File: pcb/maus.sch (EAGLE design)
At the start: 88 parts, among them Q1 BSS123, Q2 BSS123, Q3 BSS123, Q4 BSS123, Q5 BSS123, Q6 SI3499DV-T1-BE3, Q7 SI3499DV-T1-BE3, U1 ESP32-S2-WROOM, U2 CH340C, U3 CP2102, U4 LP3965EMP-3.3, U5 LSM9DS1TR, U6 LM358DR

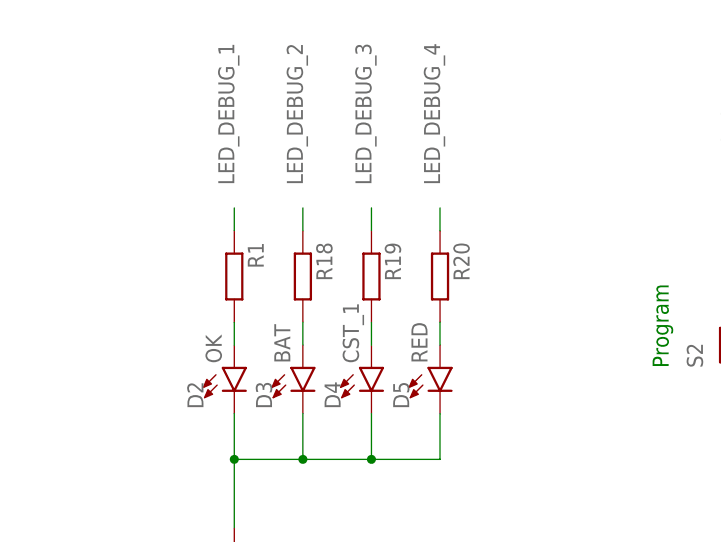
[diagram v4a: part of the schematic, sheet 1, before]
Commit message: set led resistors to 1k, fixes #10
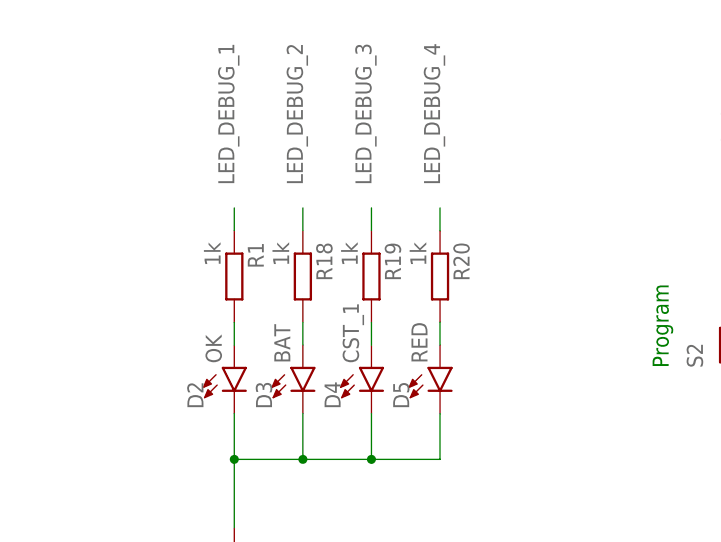
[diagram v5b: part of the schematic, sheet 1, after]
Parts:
- R1, R18, R19, R20: value (none) -> 1k
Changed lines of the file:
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@@
 <drawing>
 <settings>
-<setting alwaysvectorfont="yes"/>
+<setting alwaysvectorfont="no"/>
 <setting verticaltext="up"/>
 </settings>
@@
 <part name="D2" library="SparkFun-LED" library_urn="urn:adsk.eagle:library:529" deviceset="LED-RED" device="0603" package3d_urn="urn:adsk.eagle:package:39354/1" value="OK"/>
 <part name="GND26" library="supply1" library_urn="urn:adsk.eagle:library:371" deviceset="GND" device=""/>
-<part name="R1" library="rcl" library_urn="urn:adsk.eagle:library:334" deviceset="R-EU_" device="R0805" package3d_urn="urn:adsk.eagle:package:23553/2"/>
-<part name="R18" library="rcl" library_urn="urn:adsk.eagle:library:334" deviceset="R-EU_" device="R0805" package3d_urn="urn:adsk.eagle:package:23553/2"/>
+<part name="R1" library="rcl" library_urn="urn:adsk.eagle:library:334" deviceset="R-EU_" device="R0805" package3d_urn="urn:adsk.eagle:package:23553/2" value="1k"/>
+<part name="R18" library="rcl" library_urn="urn:adsk.eagle:library:334" deviceset="R-EU_" device="R0805" package3d_urn="urn:adsk.eagle:package:23553/2" value="1k"/>
 <part name="D3" library="SparkFun-LED" library_urn="urn:adsk.eagle:library:529" deviceset="LED-RED" device="0603" package3d_urn="urn:adsk.eagle:package:39354/1" value="BAT"/>
-<part name="R19" library="rcl" library_urn="urn:adsk.eagle:library:334" deviceset="R-EU_" device="R0805" package3d_urn="urn:adsk.eagle:package:23553/2"/>
+<part name="R19" library="rcl" library_urn="urn:adsk.eagle:library:334" deviceset="R-EU_" device="R0805" package3d_urn="urn:adsk.eagle:package:23553/2" value="1k"/>
 <part name="D4" library="SparkFun-LED" library_urn="urn:adsk.eagle:library:529" deviceset="LED-RED" device="0603" package3d_urn="urn:adsk.eagle:package:39354/1" value="CST_1"/>
-<part name="R20" library="rcl" library_urn="urn:adsk.eagle:library:334" deviceset="R-EU_" device="R0805" package3d_urn="urn:adsk.eagle:package:23553/2"/>
+<part name="R20" library="rcl" library_urn="urn:adsk.eagle:library:334" deviceset="R-EU_" device="R0805" package3d_urn="urn:adsk.eagle:package:23553/2" value="1k"/>
 <part name="D5" library="SparkFun-LED" library_urn="urn:adsk.eagle:library:529" deviceset="LED-RED" device="0603" package3d_urn="urn:adsk.eagle:package:39354/1" value="RED"/>
 <part name="C27" library="rcl" library_urn="urn:adsk.eagle:library:334" deviceset="C-EU" device="C0805" package3d_urn="urn:adsk.eagle:package:23617/2" value="0.1uF/16V"/>

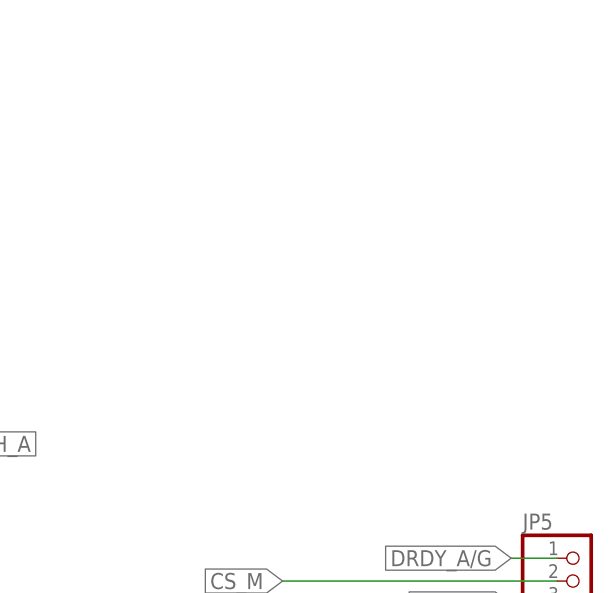
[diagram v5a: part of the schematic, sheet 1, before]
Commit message: added a SPI breakout
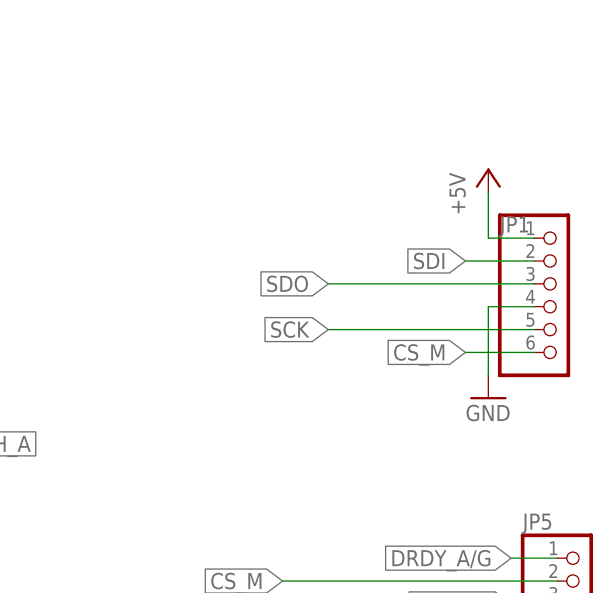
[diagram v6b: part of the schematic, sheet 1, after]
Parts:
- added JP1: (no value), pinhead:PINHD-1X6
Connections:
- net +5V: now also JP1.1
- net CS_M: now also JP1.6
- net GND: now also JP1.4
- net SCK: now also JP1.5
- net SDI: now also JP1.2
- net SDO: now also JP1.3
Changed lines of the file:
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@@
 <part name="C2" library="rcl" library_urn="urn:adsk.eagle:library:334" deviceset="C-EU" device="C0805" package3d_urn="urn:adsk.eagle:package:23617/2" value="100nF"/>
 <part name="GND40" library="supply1" library_urn="urn:adsk.eagle:library:371" deviceset="GND" device=""/>
+<part name="JP1" library="pinhead" library_urn="urn:adsk.eagle:library:325" deviceset="PINHD-1X6" device="" package3d_urn="urn:adsk.eagle:package:22472/2"/>
+<part name="P+8" library="supply1" library_urn="urn:adsk.eagle:library:371" deviceset="+5V" device=""/>
+<part name="GND43" library="supply1" library_urn="urn:adsk.eagle:library:371" deviceset="GND" device=""/>
 </parts>
 <sheets>
@@
 <instance part="+3V12" gate="G$1" x="139.7" y="200.66" smashed="yes">
 <attribute name="VALUE" x="137.16" y="195.58" size="1.778" layer="96" rot="R90"/>
+</instance>
+<instance part="JP1" gate="A" x="233.68" y="88.9" smashed="yes">
+<attribute name="NAME" x="227.33" y="97.155" size="1.778" layer="95"/>
+<attribute name="VALUE" x="227.33" y="78.74" size="1.778" layer="96"/>
+</instance>
+<instance part="P+8" gate="1" x="226.06" y="104.14" smashed="yes">
+<attribute name="VALUE" x="223.52" y="99.06" size="1.778" layer="96" rot="R90"/>
+</instance>
+<instance part="GND43" gate="1" x="226.06" y="78.74" smashed="yes">
+<attribute name="VALUE" x="223.52" y="76.2" size="1.778" layer="96"/>
 </instance>
 </instances>
@@
 <junction x="139.7" y="167.64"/>
 </segment>
+<segment>
+<pinref part="GND43" gate="1" pin="GND"/>
+<wire x1="226.06" y1="88.9" x2="226.06" y2="81.28" width="0.1524" layer="91"/>
+<pinref part="JP1" gate="A" pin="4"/>
+<wire x1="226.06" y1="88.9" x2="231.14" y2="88.9" width="0.1524" layer="91"/>
+</segment>
 </net>
 <net name="ESP32_EN" class="0">
@@
 <label x="119.38" y="58.42" size="1.778" layer="95" xref="yes"/>
 </segment>
+<segment>
+<pinref part="JP1" gate="A" pin="5"/>
+<wire x1="231.14" y1="86.36" x2="208.28" y2="86.36" width="0.1524" layer="91"/>
+<label x="208.28" y="86.36" size="1.778" layer="95" rot="R180" xref="yes"/>
+</segment>
 </net>
 <net name="SDO" class="0">
@@
 <label x="137.16" y="55.88" size="1.778" layer="95" xref="yes"/>
 </segment>
+<segment>
+<pinref part="JP1" gate="A" pin="3"/>
+<wire x1="231.14" y1="91.44" x2="208.28" y2="91.44" width="0.1524" layer="91"/>
+<label x="208.28" y="91.44" size="1.778" layer="95" rot="R180" xref="yes"/>
+</segment>
 </net>
 <net name="SDI" class="0">
@@
 <label x="137.16" y="60.96" size="1.778" layer="95" xref="yes"/>
 </segment>
+<segment>
+<pinref part="JP1" gate="A" pin="2"/>
+<wire x1="231.14" y1="93.98" x2="223.52" y2="93.98" width="0.1524" layer="91"/>
+<label x="223.52" y="93.98" size="1.778" layer="95" rot="R180" xref="yes"/>
+</segment>
 </net>
 <net name="INT" class="0">
@@
 <label x="203.2" y="58.42" size="1.778" layer="95" rot="R180" xref="yes"/>
 <wire x1="233.68" y1="58.42" x2="203.2" y2="58.42" width="0.1524" layer="91"/>
+</segment>
+<segment>
+<pinref part="JP1" gate="A" pin="6"/>
+<wire x1="231.14" y1="83.82" x2="223.52" y2="83.82" width="0.1524" layer="91"/>
+<label x="223.52" y="83.82" size="1.778" layer="95" rot="R180" xref="yes"/>
 </segment>
 </net>
@@
 </segment>
 </net>
+<net name="+5V" class="0">
+<segment>
+<pinref part="JP1" gate="A" pin="1"/>
+<pinref part="P+8" gate="1" pin="+5V"/>
+<wire x1="231.14" y1="96.52" x2="226.06" y2="96.52" width="0.1524" layer="91"/>
+<wire x1="226.06" y1="96.52" x2="226.06" y2="101.6" width="0.1524" layer="91"/>
+</segment>
+</net>

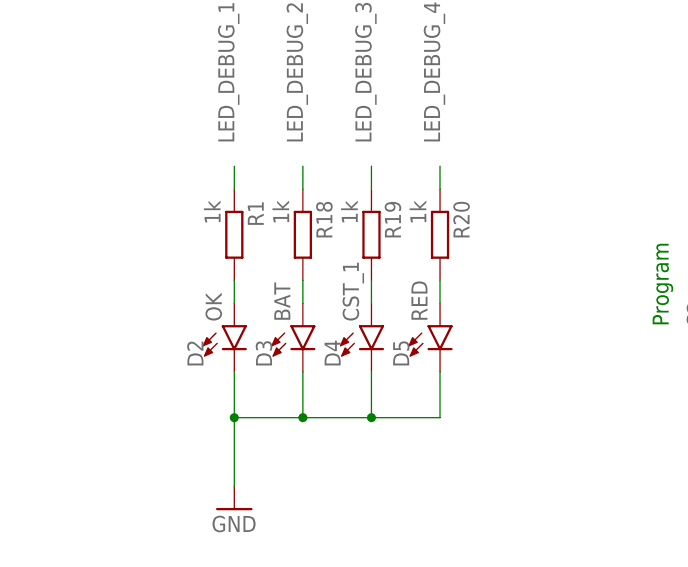
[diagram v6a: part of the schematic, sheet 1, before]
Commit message: set led 1206 package , R/C 0805. close #8
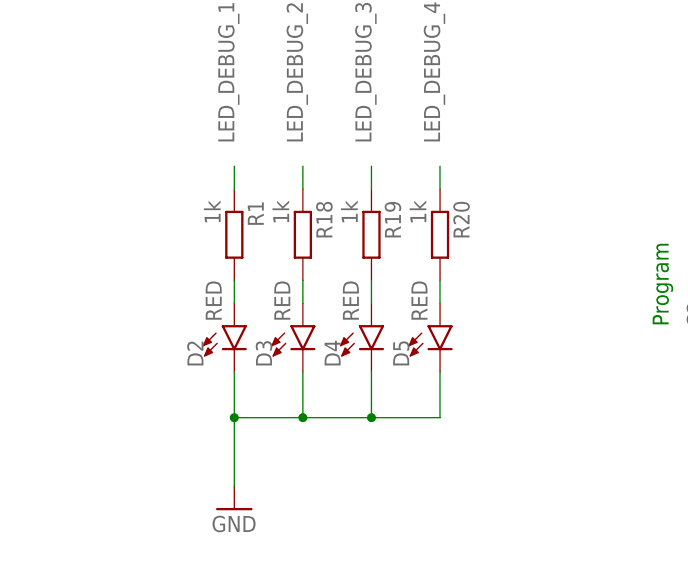
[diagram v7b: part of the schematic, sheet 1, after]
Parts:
- C10, C11, C16, C17, C18, C19: device rcl:C-EUC0603 -> rcl:C-EUC0805
- D2: value OK -> RED; device SparkFun-LED:LED-RED0603 -> SparkFun-LED:LED-RED1206
- D3: value BAT -> RED; device SparkFun-LED:LED-RED0603 -> SparkFun-LED:LED-RED1206
- D4: value CST_1 -> RED; device SparkFun-LED:LED-RED0603 -> SparkFun-LED:LED-RED1206
- D5: device SparkFun-LED:LED-RED0603 -> SparkFun-LED:LED-RED1206
- D6: value LED_RX -> RED; device SparkFun-LED:LED-RED0603 -> SparkFun-LED:LED-RED1206
- D7: value LED_TX -> RED; device SparkFun-LED:LED-RED0603 -> SparkFun-LED:LED-RED1206
- R10, R11, R12, R13, R14, R15, R16, R17, R5, R6, R7, R8, R9: device rcl:R-EU_R0603 -> rcl:R-EU_R0805

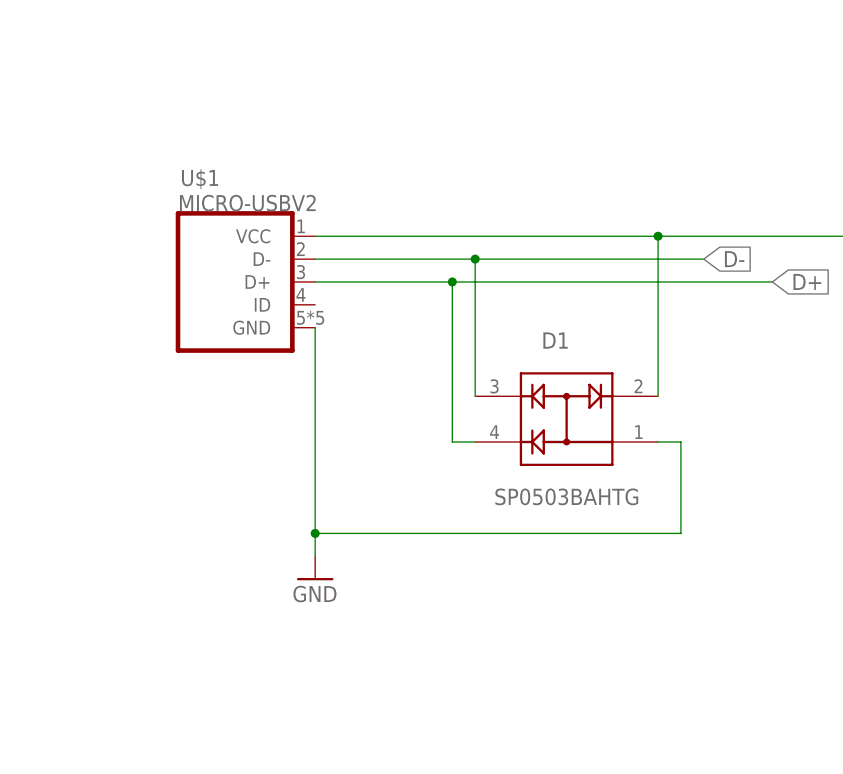
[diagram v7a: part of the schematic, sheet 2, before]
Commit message: feat: add mouser USB-B
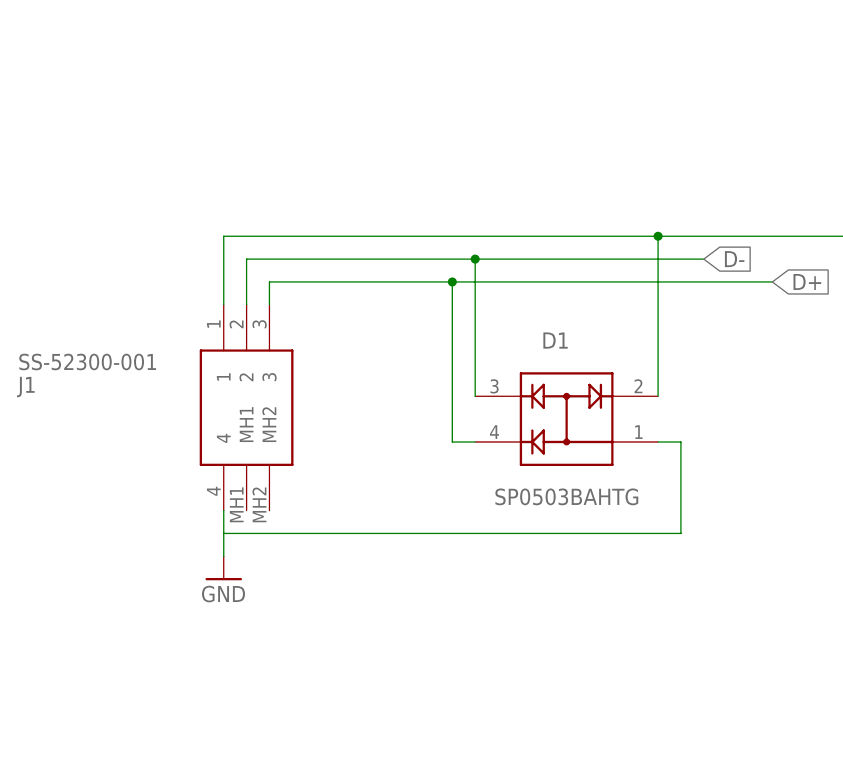
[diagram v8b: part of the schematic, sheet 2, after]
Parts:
- removed U$1: MICRO-USBV2, microusb:MICRO-USBV2
- added J1: SS-52300-001, shared:SS-52300-001
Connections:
- new net N$4: D1.1, J1.4
- net D+: now also J1.3; no longer U$1.D+
- net D-: now also J1.2; no longer U$1.D-
- net GND: no longer D1.1, U$1.GND
- net USB_VBUS: now also J1.1; no longer U$1.VCC
